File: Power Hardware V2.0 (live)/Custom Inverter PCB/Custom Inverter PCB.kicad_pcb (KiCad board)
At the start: 2 copper layers, 62 parts, among them J1 1714971, J2 1714971, J3 1714968, J4 SSQ-110-03-G-D, J5 SSQ-110-03-G-D, K1 1-1393210-3, K2 1-1393210-3, Q1 CSD19532Q5B, Q2 CSD19532Q5B, Q3 CSD19532Q5B, Q4 CSD19532Q5B, Q5 CSD19532Q5B, Q6 CSD19532Q5B, Q7 HCPL-181-06BE, Q8 HCPL-181-06BE, U1 DRV8300DIPWR, U2 NTR4170NT1G, U3 NTR4170NT1G

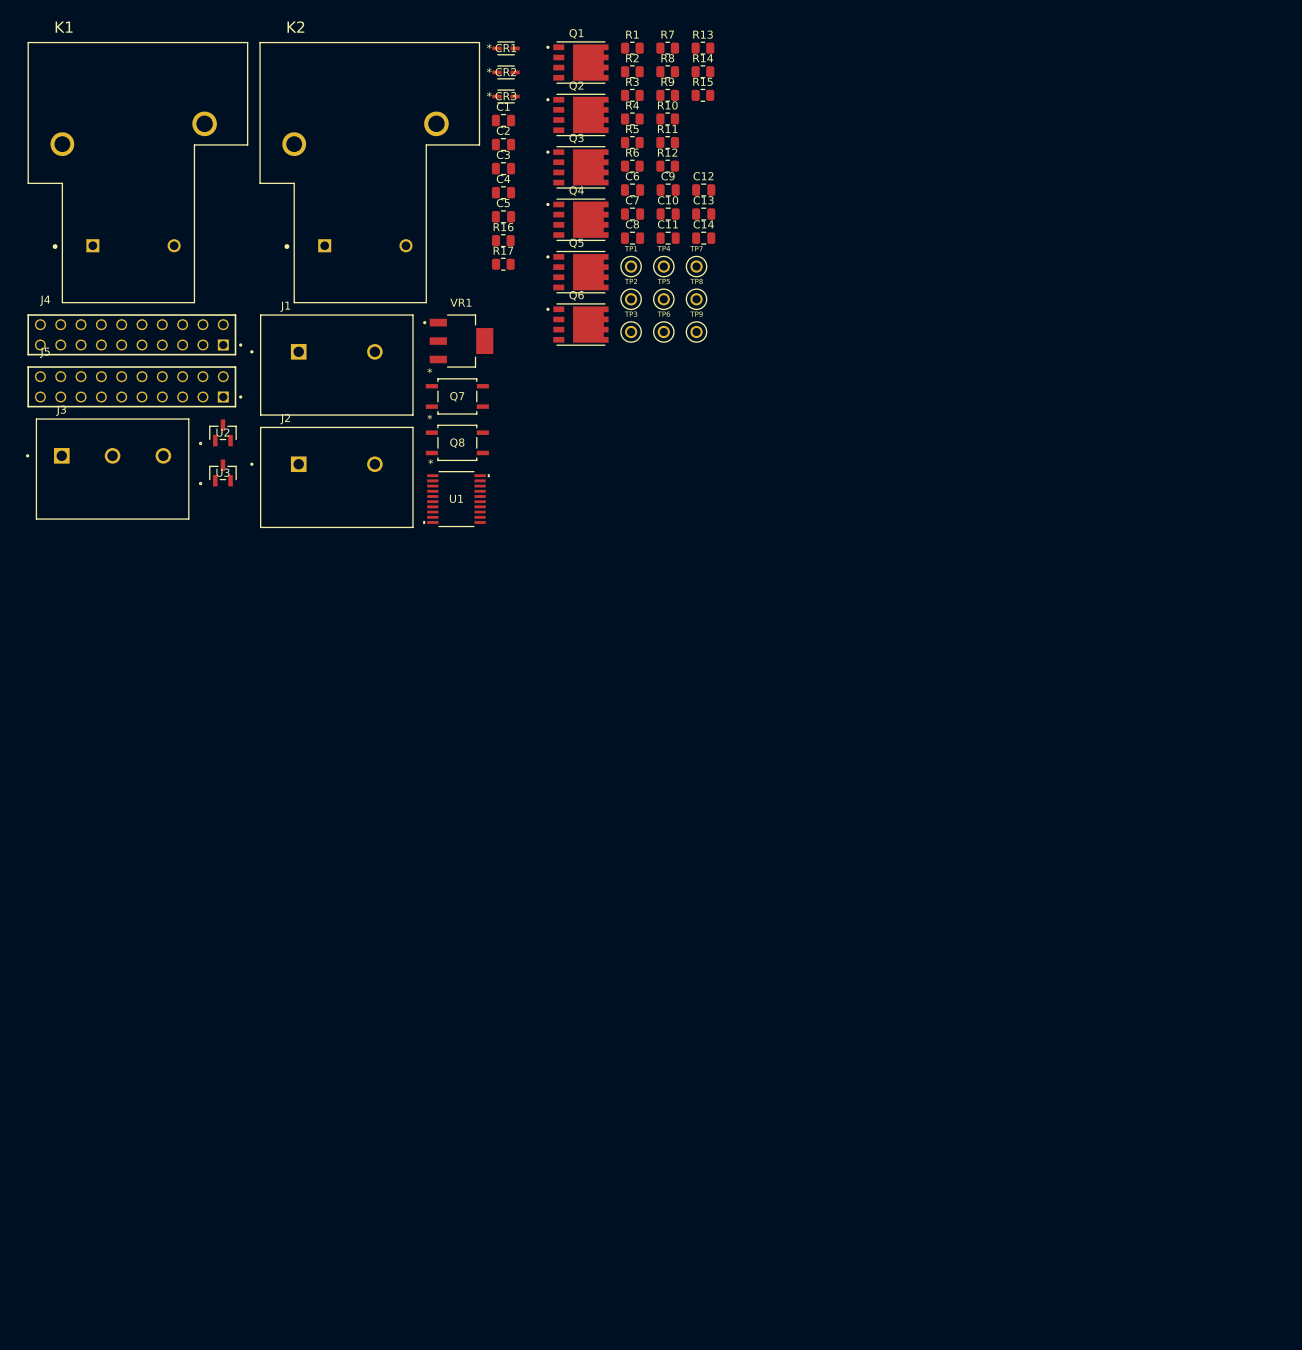
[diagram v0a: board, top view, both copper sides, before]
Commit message: switches instead of relays. Short on half bridge fixed. encoder page made. root page connections fixed
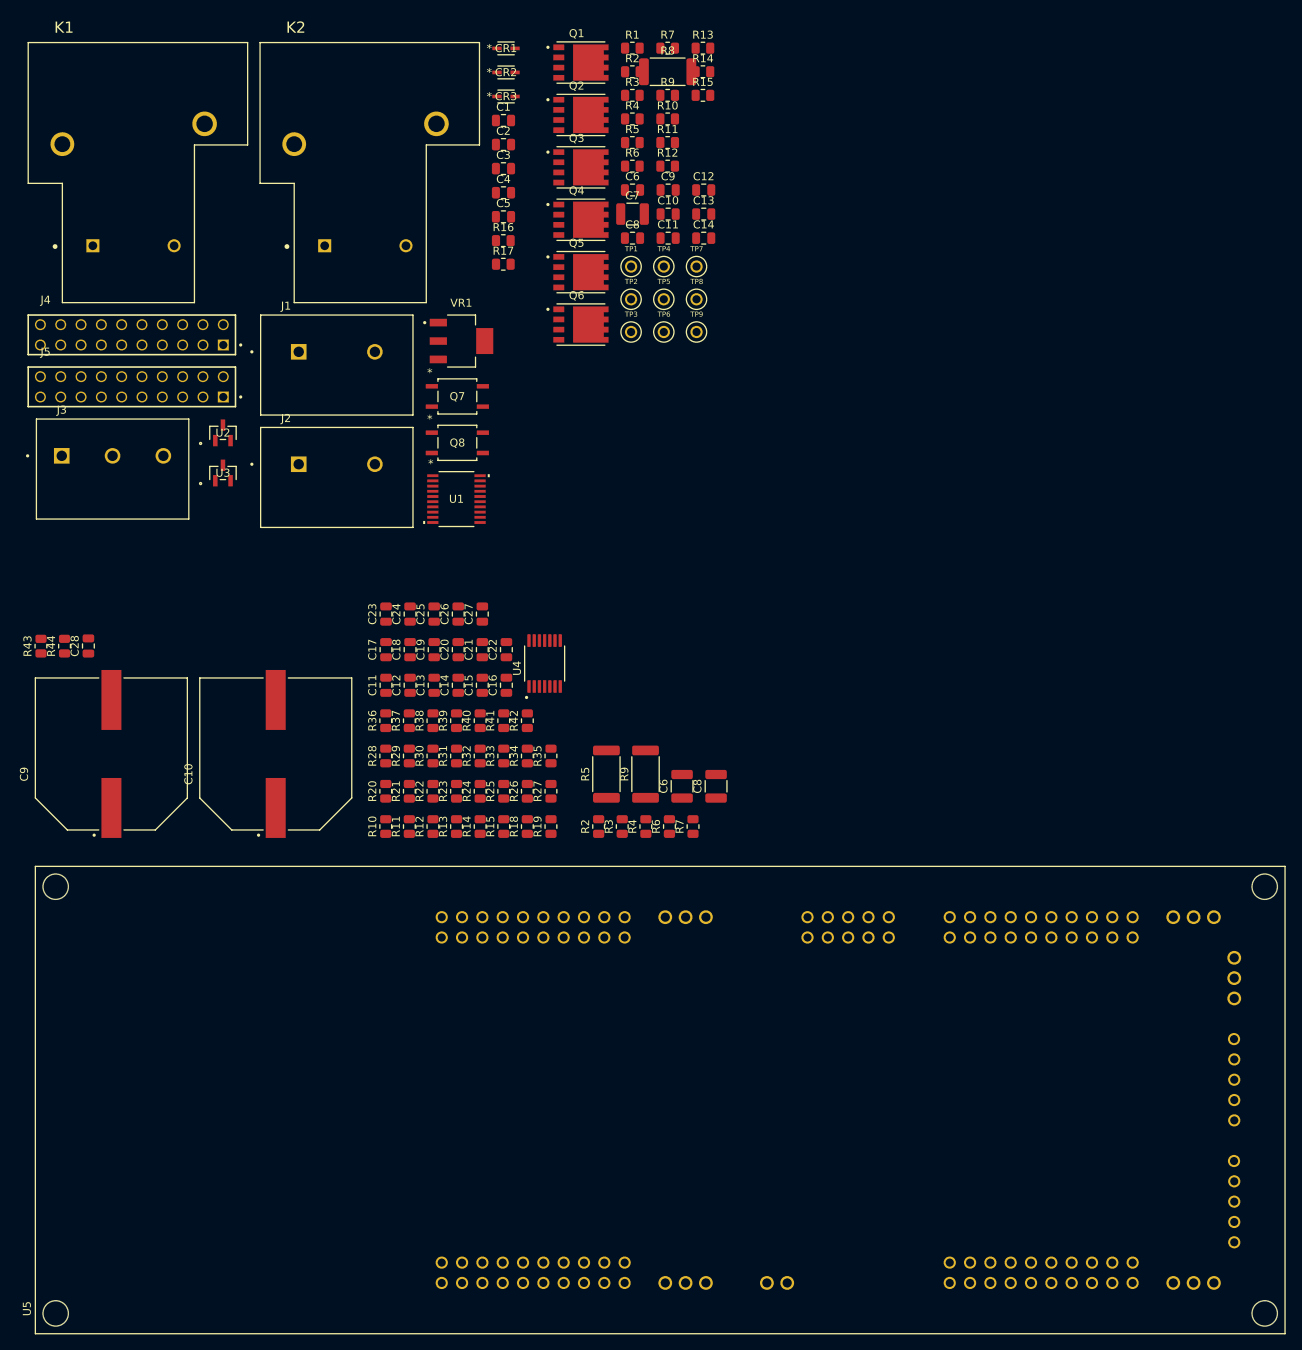
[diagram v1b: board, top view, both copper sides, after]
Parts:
- added C10: EEVFK2A331M, EEV_FK2A331M:CAP_EEVFK2A331M, F.Cu at (55.0, 116.9)
- added C11: 0.1uF, Capacitor_SMD:C_0805_2012Metric, F.Cu at (68.7, 108.3)
- added C12: 0.01uF, Capacitor_SMD:C_0805_2012Metric, F.Cu at (71.8, 108.3)
- added C13: 0.1uF, Capacitor_SMD:C_0805_2012Metric, F.Cu at (74.8, 108.3)
- added C14: 0.1uF, Capacitor_SMD:C_0805_2012Metric, F.Cu at (77.8, 108.3)
- added C15: 0.1uF, Capacitor_SMD:C_0805_2012Metric, F.Cu at (80.8, 108.3)
- added C16: 0.01uF, Capacitor_SMD:C_0805_2012Metric, F.Cu at (83.8, 108.3)
- added C17: 0.1uF, Capacitor_SMD:C_0805_2012Metric, F.Cu at (68.7, 103.9)
- added C18: 0.1uF, Capacitor_SMD:C_0805_2012Metric, F.Cu at (71.8, 103.9)
- added C19: 0.01uF, Capacitor_SMD:C_0805_2012Metric, F.Cu at (74.8, 103.9)
- added C20: 2.2uF, Capacitor_SMD:C_0805_2012Metric, F.Cu at (77.8, 103.9)
- added C21: 470pF, Capacitor_SMD:C_0805_2012Metric, F.Cu at (80.8, 103.9)
- added C22: 0.1uF, Capacitor_SMD:C_0805_2012Metric, F.Cu at (83.8, 103.9)
- added C23: 470pF, Capacitor_SMD:C_0805_2012Metric, F.Cu at (68.7, 99.4)
- added C24: 470pF, Capacitor_SMD:C_0805_2012Metric, F.Cu at (71.8, 99.4)
- added C25: 0.1uF, Capacitor_SMD:C_0805_2012Metric, F.Cu at (74.8, 99.4)
- added C26: 0.1uF, Capacitor_SMD:C_0805_2012Metric, F.Cu at (77.8, 99.4)
- added C27: 0.1uF, Capacitor_SMD:C_0805_2012Metric, F.Cu at (80.8, 99.4)
- added C28: 0.1uF, Capacitor_SMD:C_0805_2012Metric, F.Cu at (31.5, 103.4)
- added C6: 1uF, Capacitor_SMD:C_1210_3225Metric, F.Cu at (105.8, 121.0)
- added C8: 1uF, Capacitor_SMD:C_1210_3225Metric, F.Cu at (110.0, 121.0)
- added C9: EEVFK2A331M, EEV_FK2A331M:CAP_EEVFK2A331M, F.Cu at (34.4, 116.9)
- added R10: 10K, Resistor_SMD:R_0805_2012Metric, F.Cu at (68.7, 126.0)
- added R11: 10K, Resistor_SMD:R_0805_2012Metric, F.Cu at (71.7, 126.0)
- added R12: 4.99K, Resistor_SMD:R_0805_2012Metric, F.Cu at (74.6, 126.0)
- added R13: 4.99K, Resistor_SMD:R_0805_2012Metric, F.Cu at (77.6, 126.0)
- added R14: 100k, Resistor_SMD:R_0805_2012Metric, F.Cu at (80.5, 126.0)
- added R15: 49.9K, Resistor_SMD:R_0805_2012Metric, F.Cu at (83.5, 126.0)
- added R18: 100k, Resistor_SMD:R_0805_2012Metric, F.Cu at (86.4, 126.0)
- added R19: 10K, Resistor_SMD:R_0805_2012Metric, F.Cu at (89.4, 126.0)
- added R2: 15R, Resistor_SMD:R_0805_2012Metric, F.Cu at (95.3, 126.0)
- added R20: 49.9K, Resistor_SMD:R_0805_2012Metric, F.Cu at (68.7, 121.6)
- added R21: 10K, Resistor_SMD:R_0805_2012Metric, F.Cu at (71.7, 121.6)
- added R22: 4.99K, Resistor_SMD:R_0805_2012Metric, F.Cu at (74.6, 121.6)
- added R23: 4.99K, Resistor_SMD:R_0805_2012Metric, F.Cu at (77.6, 121.6)
- added R24: 49.9K, Resistor_SMD:R_0805_2012Metric, F.Cu at (80.5, 121.6)
- added R25: 49.9K, Resistor_SMD:R_0805_2012Metric, F.Cu at (83.5, 121.6)
- added R26: 10K, Resistor_SMD:R_0805_2012Metric, F.Cu at (86.4, 121.6)
- added R27: 10K, Resistor_SMD:R_0805_2012Metric, F.Cu at (89.4, 121.6)
- added R28: 4.99K, Resistor_SMD:R_0805_2012Metric, F.Cu at (68.7, 117.2)
- added R29: 4.99K, Resistor_SMD:R_0805_2012Metric, F.Cu at (71.7, 117.2)
- added R3: 15R, Resistor_SMD:R_0805_2012Metric, F.Cu at (98.3, 126.0)
- added R30: 49.9K, Resistor_SMD:R_0805_2012Metric, F.Cu at (74.6, 117.2)
- added R31: 49.9K, Resistor_SMD:R_0805_2012Metric, F.Cu at (77.6, 117.2)
- added R32: 330R, Resistor_SMD:R_0805_2012Metric, F.Cu at (80.5, 117.2)
- added R33: 97.6K, Resistor_SMD:R_0805_2012Metric, F.Cu at (83.5, 117.2)
- added R34: 3K, Resistor_SMD:R_0805_2012Metric, F.Cu at (86.4, 117.2)
- added R35: 330R, Resistor_SMD:R_0805_2012Metric, F.Cu at (89.4, 117.2)
- added R36: 330R, Resistor_SMD:R_0805_2012Metric, F.Cu at (68.7, 112.8)
- added R37: 97.6K, Resistor_SMD:R_0805_2012Metric, F.Cu at (71.7, 112.8)
- added R38: 3K, Resistor_SMD:R_0805_2012Metric, F.Cu at (74.6, 112.8)
- added R39: 97.6K, Resistor_SMD:R_0805_2012Metric, F.Cu at (77.6, 112.8)
- added R4: 15R, Resistor_SMD:R_0805_2012Metric, F.Cu at (101.2, 126.0)
- added R40: 3K, Resistor_SMD:R_0805_2012Metric, F.Cu at (80.5, 112.8)
- added R41: 97.6K, Resistor_SMD:R_0805_2012Metric, F.Cu at (83.5, 112.8)
- added R42: 3K, Resistor_SMD:R_0805_2012Metric, F.Cu at (86.4, 112.8)
- added R43: 97.6K, Resistor_SMD:R_0805_2012Metric, F.Cu at (25.6, 103.5)
- added R44: 3K, Resistor_SMD:R_0805_2012Metric, F.Cu at (28.6, 103.5)
- added R5: 0.003R, Resistor_SMD:R_2512_6332Metric, F.Cu at (96.3, 119.5)
- added R6: 15R, Resistor_SMD:R_0805_2012Metric, F.Cu at (104.2, 126.0)
- added R7: 15R, Resistor_SMD:R_0805_2012Metric, F.Cu at (107.1, 126.0)
- added R9: 0.003R, Resistor_SMD:R_2512_6332Metric, F.Cu at (101.2, 119.5)
- added U4: TLV9004IPWR, TLV9004IPWR:SOP65P640X120-14N, F.Cu at (88.6, 105.6)
- added U5: LAUNCHXL-F280049C, LAUNCHXL-F280049C:MODULE_LAUNCHXL-F280049C, F.Cu at (103.0, 160.2)
- C7: value C -> 1uF; footprint Capacitor_SMD:C_0805_2012Metric -> Capacitor_SMD:C_1210_3225Metric
- R1: value R -> 15R
- R8: value R -> 0.003R; footprint Resistor_SMD:R_0805_2012Metric -> Resistor_SMD:R_2512_6332Metric
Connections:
- C1 pad 2: GND -> +100VDC
- C2 pad 2: GND -> +100VDC
- C3 pad 2: /GateDriver&Power Inputs/MOTA -> +100VDC
- C4 pad 2: /GateDriver&Power Inputs/MOTB -> +100VDC
- C5 pad 2: /GateDriver&Power Inputs/MOTC -> +100VDC
- C7 pad 2: GND -> +100VDC
- J1 pad 1: GND -> +100VDC
- J2 pad 1: GND -> +100VDC
- J2 pad 2: +100VDC to Relay -> Net-(F1-Pad1)
- J3 pad 1: /GateDriver&Power Inputs/MOTA -> +100VDC
- J3 pad 2: /GateDriver&Power Inputs/MOTB -> +100VDC
- J3 pad 3: /GateDriver&Power Inputs/MOTC -> +100VDC
- J4 pad 04: GND -> +100VDC
- J4 pad 06: unconnected-(J4-Pad06) -> /GateDriver&Power Inputs/VSENA
- J4 pad 08: unconnected-(J4-Pad08) -> /GateDriver&Power Inputs/VSENB
- J4 pad 10: unconnected-(J4-Pad10) -> /GateDriver&Power Inputs/VSENC
- J4 pad 12: unconnected-(J4-Pad12) -> /GateDriver&Power Inputs/SEN_100V
- J4 pad 14: unconnected-(J4-Pad14) -> /GateDriver&Power Inputs/ISENC
- J4 pad 16: unconnected-(J4-Pad16) -> /GateDriver&Power Inputs/ISENB
- J4 pad 18: unconnected-(J4-Pad18) -> /GateDriver&Power Inputs/ISENA
- J4 pad 20: unconnected-(J4-Pad20) -> /GateDriver&Power Inputs/VSEN_12V
- J5 pad 02: GND -> +100VDC
- Q1 pad 1: /GateDriver&Power Inputs/MOTA -> +100VDC
- Q2 pad 5_8: /GateDriver&Power Inputs/MOTA -> +100VDC
- Q3 pad 1: /GateDriver&Power Inputs/MOTB -> +100VDC
- Q4 pad 5_8: /GateDriver&Power Inputs/MOTB -> +100VDC
- Q5 pad 1: /GateDriver&Power Inputs/MOTC -> +100VDC
- Q6 pad 5_8: /GateDriver&Power Inputs/MOTC -> +100VDC
- Q7 pad 4: GND -> +100VDC
- Q8 pad 4: GND -> +100VDC
- R16 pad 1: GND -> +100VDC
- R17 pad 1: GND -> +100VDC
- R8 pad 2: GND -> +100VDC
- TP1 pad TP: /GateDriver&Power Inputs/MOTA -> +100VDC
- TP6 pad TP: /GateDriver&Power Inputs/MOTB -> +100VDC
- TP9 pad TP: /GateDriver&Power Inputs/MOTC -> +100VDC
- U1 pad 12: /GateDriver&Power Inputs/MOTC -> +100VDC
- U1 pad 15: /GateDriver&Power Inputs/MOTB -> +100VDC
- U1 pad 18: /GateDriver&Power Inputs/MOTA -> +100VDC
- U1 pad 8: GND -> +100VDC
- U2 pad 2: GND -> +100VDC
- U3 pad 2: GND -> +100VDC
- VR1 pad 2: GND -> +100VDC
- VR1 pad 4: GND -> +100VDC

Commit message: Schematic Changes
-Changed 3.3V regulator to a higher power unit for the sin-cos circuit (from 500mA to 3A)
-Fixed flipped MOTA,B,C connection to Output Terminal
- Current Sense IC setup
- Fuses for Phase current outputs
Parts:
- moved J4 158.6 mm to (194.3, 44.2)
- moved U5 134.6 mm to (211.5, 80.5)

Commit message: no changes
no
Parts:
- added C11: 220nF, Capacitor_SMD:C_0603_1608Metric_Pad1.08x0.95mm_HandSolder, F.Cu at (119.0, 80.6)
- added C12: 220nF, Capacitor_SMD:C_0603_1608Metric_Pad1.08x0.95mm_HandSolder, F.Cu at (119.0, 83.1)
- added C13: 220nF, Capacitor_SMD:C_0603_1608Metric_Pad1.08x0.95mm_HandSolder, F.Cu at (119.0, 85.6)
- added C14: 220nF, Capacitor_SMD:C_0603_1608Metric_Pad1.08x0.95mm_HandSolder, F.Cu at (119.0, 88.1)
- added R10: 4.7K, Resistor_SMD:R_0805_2012Metric, F.Cu at (114.6, 80.8)
- added R11: 4.7K, Resistor_SMD:R_0805_2012Metric, F.Cu at (114.6, 83.8)
- added R12: 4.7K, Resistor_SMD:R_0805_2012Metric, F.Cu at (114.6, 86.7)
- added R13: 4.7K, Capacitor_SMD:C_0603_1608Metric_Pad1.08x0.95mm_HandSolder, F.Cu at (119.0, 90.6)
- added R14: 4.7K, Resistor_SMD:R_0805_2012Metric, F.Cu at (114.6, 89.7)
- added R15: 4.7K, Resistor_SMD:R_0805_2012Metric, F.Cu at (114.6, 92.6)
- added R16: 4.7K, Resistor_SMD:R_0805_2012Metric, F.Cu at (114.6, 95.5)
- added R17: 4.7K, Resistor_SMD:R_0805_2012Metric, F.Cu at (114.6, 98.5)
- C21, C23, C24: value 470pF -> 47nF
- R32, R35, R36: value 330R -> 220R
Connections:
- net Net-(U5B-+5V0-PadJ12_4) renamed +5V
- C1 pad 1: +3.3V -> +3.3VDC
- C1 pad 2: +100VDC -> GND
- C10 pad 2: +100VDC -> GND
- C2 pad 1: +12V -> +12VDC
- C2 pad 2: +100VDC -> GND
- C28 pad 1: /GateDriver&Power Inputs/SEN_100V -> /SEN_100V
- C28 pad 2: +100VDC -> GND
- C3 pad 2: +100VDC -> /SHA
- C4 pad 2: +100VDC -> /SHB
- C5 pad 2: +100VDC -> /SHC
- C6 pad 2: +100VDC -> GND
- C7 pad 2: +100VDC -> GND
- C8 pad 2: +100VDC -> GND
- C9 pad 2: +100VDC -> GND
- CR1 pad 2: +12V -> +12VDC
- CR2 pad 2: +12V -> +12VDC
- CR3 pad 2: +12V -> +12VDC
- J1 pad 1: +100VDC -> GND
- J1 pad 2: +12V - to relay -> +12V to relay
- J2 pad 1: +100VDC -> GND
- J3 pad 1: +100VDC -> /MOTA
- J3 pad 2: +100VDC -> /MOTB
- J3 pad 3: +100VDC -> /MOTC
- K2 pad A1: +12V - to relay -> Net-(J7-Pad1)
- K2 pad A2: Net-(U3-DRAIN) -> GND
- Q1 pad 1: +100VDC -> /SHA
- Q2 pad 1: /Half_Bridges/SAHI -> GND
- Q2 pad 5_8: +100VDC -> /SHA
- Q3 pad 1: +100VDC -> /SHB
- Q4 pad 1: /Half_Bridges/SBHI -> GND
- Q4 pad 5_8: +100VDC -> /SHB
- Q5 pad 1: +100VDC -> /SHC
- Q6 pad 1: /Half_Bridges/SCHI -> GND
- Q6 pad 5_8: +100VDC -> /SHC
- R43 pad 2: /GateDriver&Power Inputs/SEN_100V -> /SEN_100V
- R44 pad 1: /GateDriver&Power Inputs/SEN_100V -> /SEN_100V
- R44 pad 2: +100VDC -> GND
- TP1 pad TP: +100VDC -> /MOTA
- TP6 pad TP: +100VDC -> /MOTB
- TP9 pad TP: +100VDC -> /MOTC
- U1 pad 1: /GateDriver&Power Inputs/INHA -> /INHA
- U1 pad 12: +100VDC -> /SHC
- U1 pad 15: +100VDC -> /SHB
- U1 pad 18: +100VDC -> /SHA
- U1 pad 2: /GateDriver&Power Inputs/INHB -> /INHB
- U1 pad 3: /GateDriver&Power Inputs/INHC -> /INHC
- U1 pad 4: /GateDriver&Power Inputs/INLA -> /INLA
- U1 pad 5: /GateDriver&Power Inputs/INLB -> /INLC
- U1 pad 6: /GateDriver&Power Inputs/INLC -> /INLC
- U1 pad 7: +12V -> +12VDC
- U1 pad 8: +100VDC -> GND
- U5 pad J11_10: Net-(U5B-+3.3V-PadJ11_10) -> +3.3V
- U5 pad J11_3: Net-(U5B-GND_1-PadJ11_3) -> GND
- U5 pad J11_4: Net-(U5B-GND_1-PadJ11_3) -> GND
- U5 pad J12_5: Net-(U5B-GND_1-PadJ11_3) -> GND
- U5 pad J13_5: Net-(U5B-GND_1-PadJ11_3) -> GND
- U5 pad J14_3: Net-(U5B-GND_1-PadJ11_3) -> GND
- U5 pad J15_2: Net-(U5B-GND_2-PadJ15_2) -> GND
- U5 pad J1_1: Net-(U5B-+3.3V-PadJ11_10) -> +3.3V
- U5 pad J2_20: Net-(U5B-GND_1-PadJ11_3) -> GND
- U5 pad J3_22: Net-(U5B-GND_1-PadJ11_3) -> GND
- U5 pad J6_60: Net-(U5B-GND_1-PadJ11_3) -> GND
- U5 pad J7_62: Net-(U5B-GND_1-PadJ11_3) -> GND
- U5 pad JP4_1: Net-(U5B-+3.3V-PadJ11_10) -> +3.3V
- U5 pad JP4_2: Net-(U5B-GND_2-PadJ15_2) -> GND
- U5 pad JP4_3: Net-(U5B-GND_2-PadJ15_2) -> GND
- U5 pad JP5_2: Net-(U5B-GND_2-PadJ15_2) -> GND
- U5 pad JP5_3: Net-(U5B-GND_2-PadJ15_2) -> GND
- U5 pad JP6_1: Net-(U5B-+3.3V-PadJ11_10) -> +3.3V
- U5 pad JP6_2: Net-(U5B-GND_2-PadJ15_2) -> GND
- U5 pad JP6_3: Net-(U5B-GND_2-PadJ15_2) -> GND
- U5 pad JP7_2: Net-(U5B-GND_2-PadJ15_2) -> GND
- U5 pad JP7_3: Net-(U5B-GND_2-PadJ15_2) -> GND
